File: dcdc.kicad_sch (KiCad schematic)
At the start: 59 parts, among them J301 Conn_01x01, J302 Conn_01x01, J303 Conn_01x01, J304 Conn_01x01, J305 Conn_01x01, Q301 MMBT3904, T301 Feryster RTN-40x25x15(M-083), U301 L78L33_SOT89, U302 LT3439, U303 24AA02-OT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

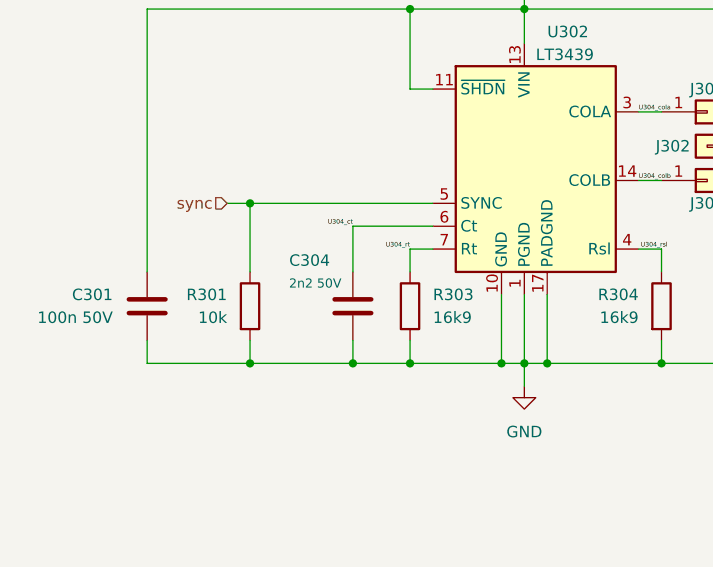
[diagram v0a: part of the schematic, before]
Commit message: adding prec resistor alternatives
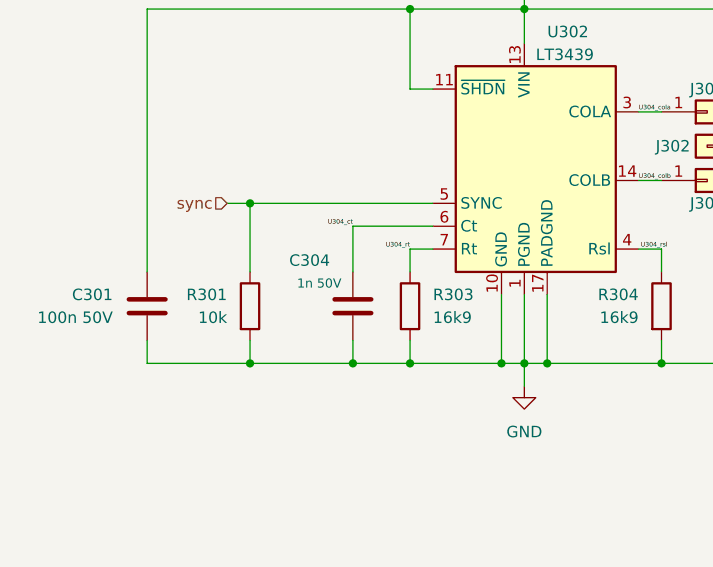
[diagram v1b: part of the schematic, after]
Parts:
- C304: value 2n2 50V -> 1n 50V
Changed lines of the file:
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@@
       (effects (font (size 1.27 1.27)) (justify right))
     )
-    (property "Value" "2n2 50V" (id 1) (at 46.99 102.87 0)
+    (property "Value" "1n 50V" (id 1) (at 46.99 102.87 0)
       (effects (font (size 1.016 1.016)) (justify right))
     )

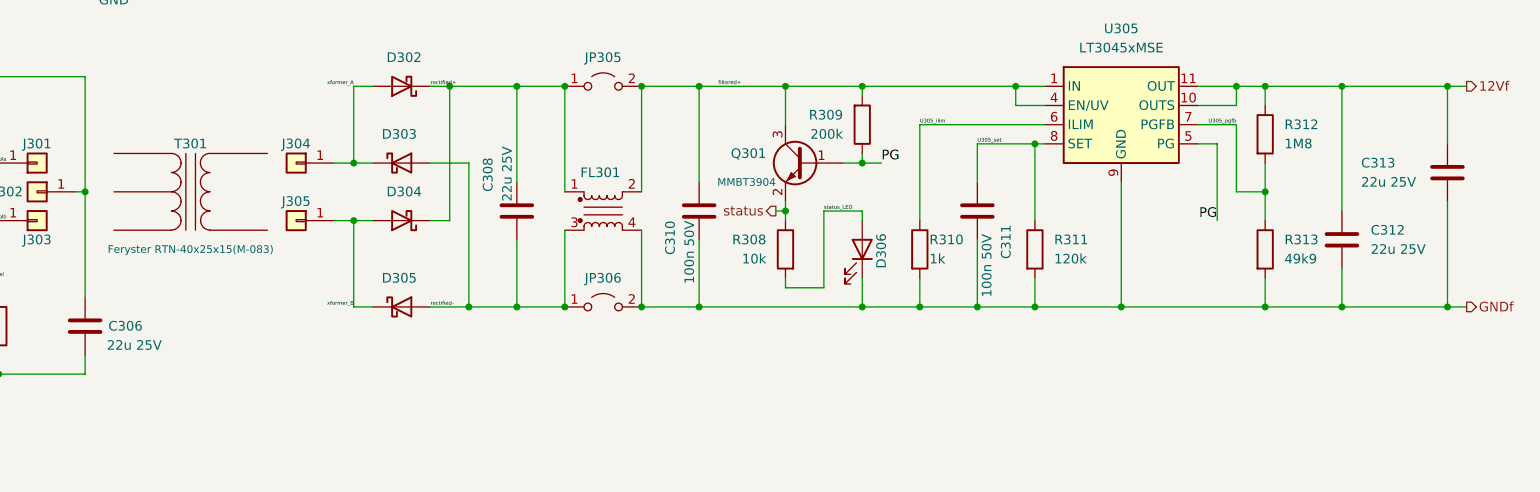
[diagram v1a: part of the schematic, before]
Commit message: goodbye proto area, hello resistor networks
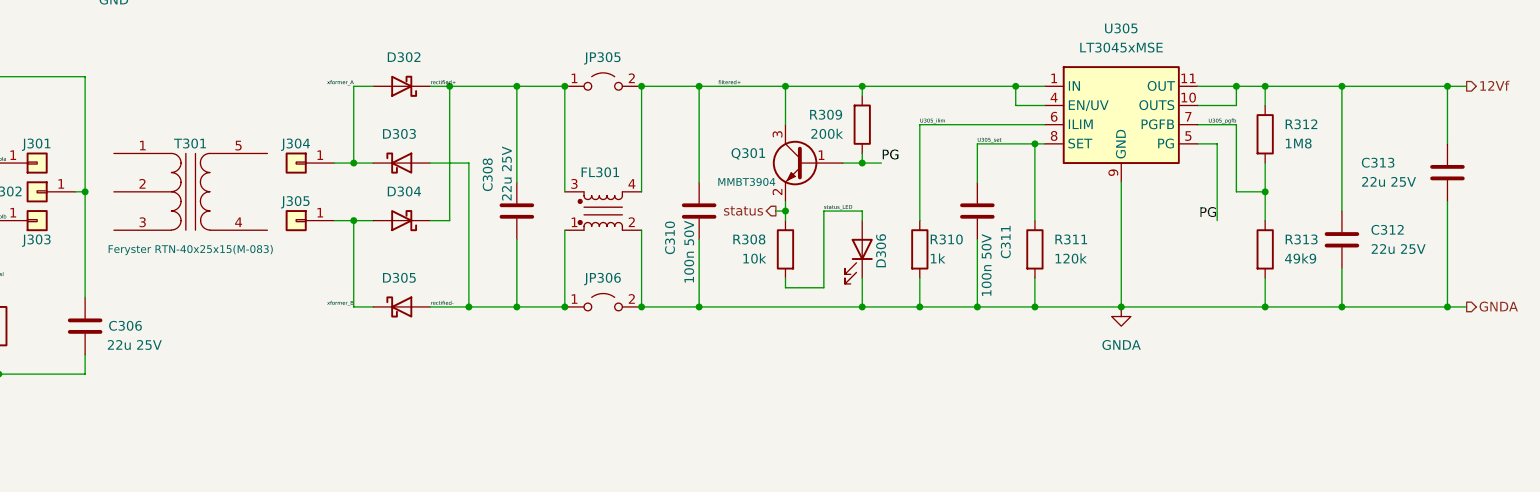
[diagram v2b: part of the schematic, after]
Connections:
- net filtered+: now also FL301.4; no longer FL301.2
- net rectified+: now also FL301.3; no longer FL301.1
- net rectified-: now also FL301.1; no longer FL301.3
- net GNDf renamed GNDA
- net GNDA: now also FL301.2; no longer FL301.4
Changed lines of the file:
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@@
     (effects (font (size 0.5 0.5)) (justify right bottom))
   )
-  (hierarchical_label "GNDf" (shape output) (at 276.86 102.87 0)
+  (hierarchical_label "GNDA" (shape output) (at 276.86 102.87 0)
     (effects (font (size 1.27 1.27)) (justify left))
   )
@@
     (pin "1")
   )
-  (symbol (lib_id "Device:Filter_EMI_CommonMode") (at 162.56 90.17 0) (unit 1)
+  (symbol (lib_id "Device:Filter_EMI_CommonMode") (at 162.56 90.17 0) (mirror x) (unit 1)
     (in_bom yes) (on_board yes) (fields_autoplaced)
     (property "Reference" "FL301" (id 0) (at 162.179 85.09 0))
-    (property "Value" "B82793C0206N265" (id 1) (at 162.179 85.09 0)
-      (effects (font (size 1.27 1.27)) hide)
-    )
-    (property "Footprint" "ADRmu_Library:Filter_EPCOS_B82793C0" (id 2) (at 162.56 89.154 0)
-      (effects (font (size 1.27 1.27)) hide)
-    )
-    (property "Datasheet" "~" (id 3) (at 162.56 89.154 0)
+    (property "Value" "B82793C0206N265" (id 1) (at 162.179 95.25 0)
+      (effects (font (size 1.27 1.27)) hide)
+    )
+    (property "Footprint" "ADRmu_Library:Filter_EPCOS_B82793C0" (id 2) (at 162.56 91.186 0)
+      (effects (font (size 1.27 1.27)) hide)
+    )
+    (property "Datasheet" "~" (id 3) (at 162.56 91.186 0)
       (effects (font (size 1.27 1.27)) hide)
     )
@@
     (pin "9")
   )
+  (symbol (lib_id "power:GNDA") (at 231.14 102.87 0) (unit 1)
+    (in_bom yes) (on_board yes) (fields_autoplaced)
+    (property "Reference" "#PWR0101" (id 0) (at 231.14 109.22 0)
+      (effects (font (size 1.27 1.27)) hide)
+    )
+    (property "Value" "GNDA" (id 1) (at 231.14 107.95 0))
+    (property "Footprint" "" (id 2) (at 231.14 102.87 0)
+      (effects (font (size 1.27 1.27)) hide)
+    )
+    (property "Datasheet" "" (id 3) (at 231.14 102.87 0)
+      (effects (font (size 1.27 1.27)) hide)
+    )
+    (pin "1")
+  )
   (symbol (lib_id "Device:C") (at 274.32 85.09 0) (unit 1)

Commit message: Rev 0.3
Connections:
- net U304_cola renamed U302_cola
- net U304_colb renamed U302_colb
- net U304_ct renamed U302_ct
- net U304_rsl renamed U302_rsl
- net U304_rt renamed U302_rt
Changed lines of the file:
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@@
     (stroke (width 0) (type default) (color 0 0 0 0))
   )
-  (label "U304_rt" (at 54.61 99.06 180)
+  (label "U302_rt" (at 54.61 99.06 180)
     (effects (font (size 0.5 0.5)) (justify right bottom))
   )
@@
     (effects (font (size 0.5 0.5)) (justify left bottom))
   )
-  (label "U304_cola" (at 80.01 83.82 0)
+  (label "U302_cola" (at 80.01 83.82 0)
     (effects (font (size 0.5 0.5)) (justify left bottom))
   )
@@
     (effects (font (size 0.5 0.5)) (justify right bottom))
   )
-  (label "U304_rsl" (at 80.2368 99.06 0)
+  (label "U302_rsl" (at 80.2368 99.06 0)
     (effects (font (size 0.5 0.5)) (justify left bottom))
   )
@@
     (effects (font (size 1.27 1.27)) (justify right bottom))
   )
-  (label "U304_colb" (at 80.01 91.44 0)
+  (label "U302_colb" (at 80.01 91.44 0)
     (effects (font (size 0.5 0.5)) (justify left bottom))
   )
@@
     (effects (font (size 1.27 1.27)) (justify left bottom))
   )
-  (label "U304_ct" (at 48.26 96.52 180)
+  (label "U302_ct" (at 48.26 96.52 180)
     (effects (font (size 0.5 0.5)) (justify right bottom))
   )
